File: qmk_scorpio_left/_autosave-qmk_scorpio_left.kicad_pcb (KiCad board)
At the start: 2 copper layers, 174.2 x 117.5 mm, 149 parts, among them J1 USB_C_Receptacle_USB2.0, J2 Conn_01x05, J3 USB_C_Receptacle_USB2.0, Q3 MMUN2133LT1G, U1 STM32G474CETx, U2 PRTR5V0U2X, U3 XC6206PxxxMR-Regulator_Linear, U4 CR2013-MI2120, U5 PRTR5V0U2X

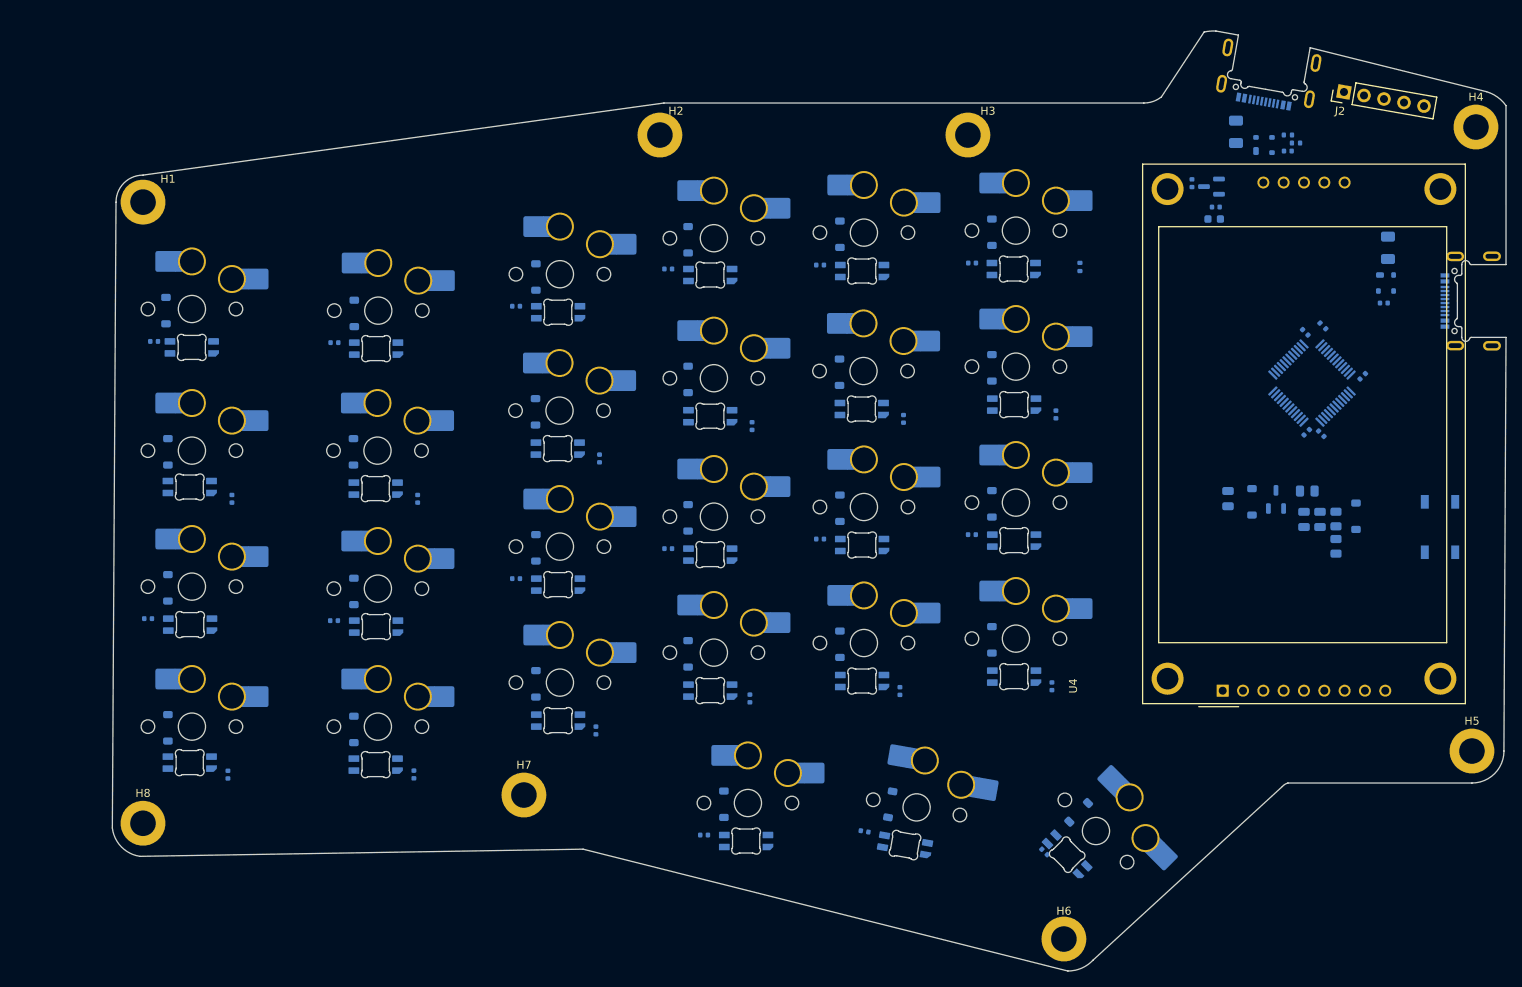
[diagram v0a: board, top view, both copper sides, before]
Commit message: fixed annular width drc error
increased pad diameter from 3.3 mm to 3.5 mm
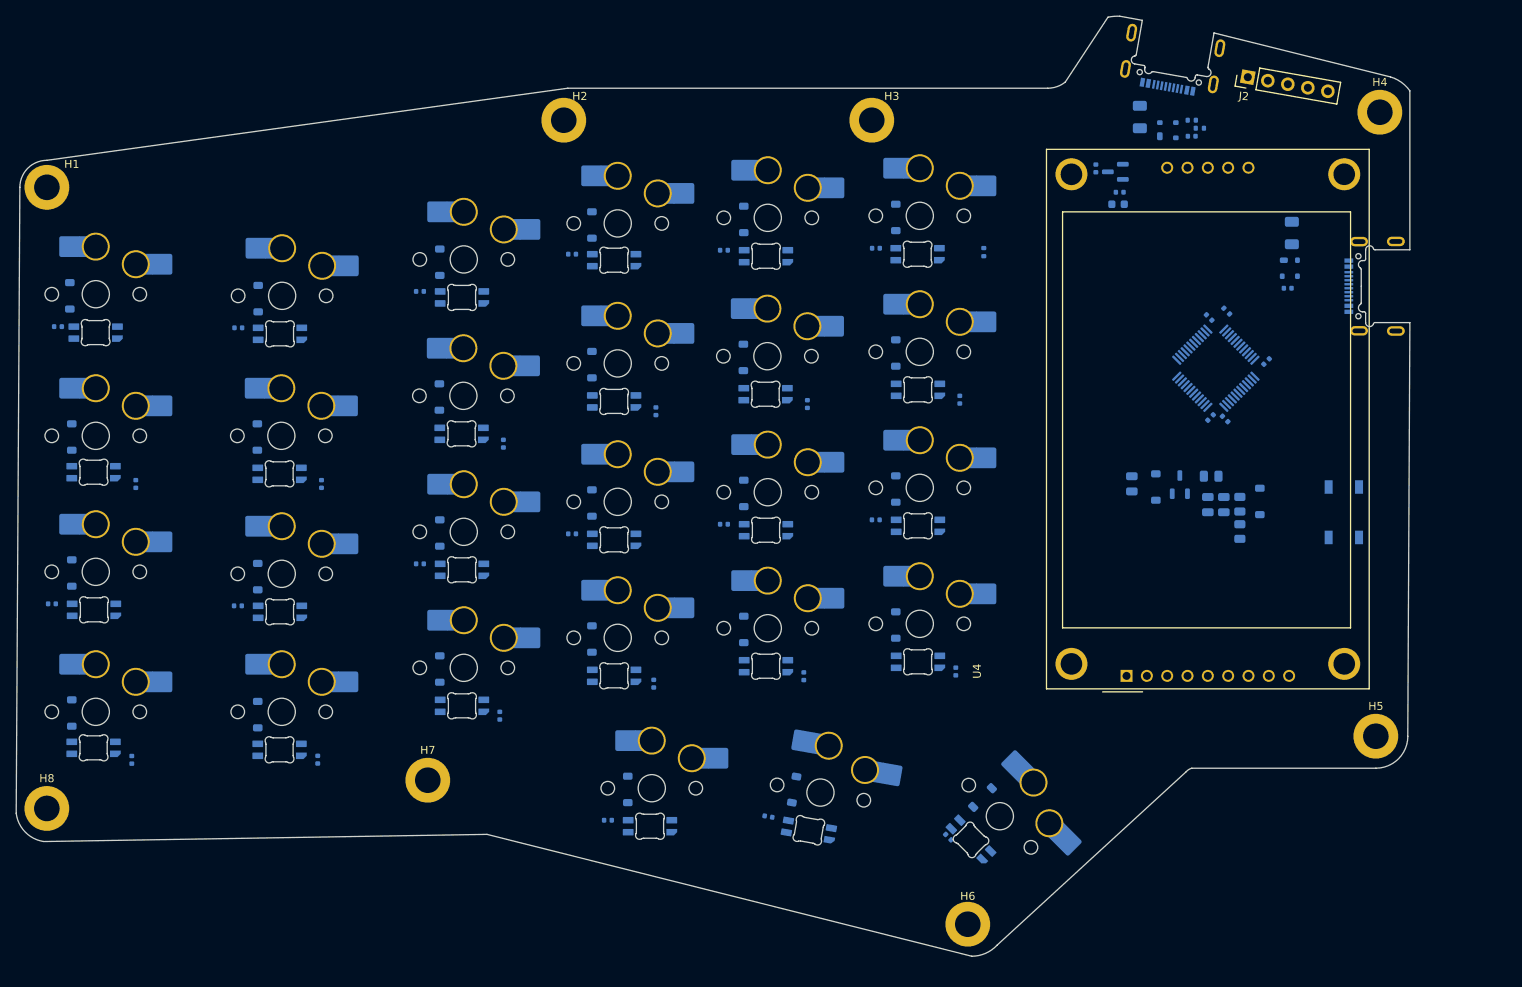
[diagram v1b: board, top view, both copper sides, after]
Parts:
- moved C27 12.2 mm to (179.6, 135.8)
- moved LED27 12.2 mm to (182.4, 136.1)
- moved C1 12.2 mm to (68.3, 72.0)
- moved C10 12.2 mm to (143.0, 82.5)
- moved C101 12.2 mm to (200.8, 56.6)
- moved C106 12.2 mm to (198.0, 52.2)
- moved C12 12.2 mm to (181.0, 81.1)
- moved C17 12.2 mm to (151.5, 96.7)
- moved C18 12.2 mm to (170.5, 96.1)
- moved C22 12.2 mm to (142.7, 116.6)
- moved C23 12.2 mm to (161.5, 115.7)
- moved C24 12.2 mm to (180.5, 115.1)
- moved C25 12.2 mm to (137.0, 133.7)
- moved C41 12.2 mm to (214.0, 94.2)
- moved C42 12.2 mm to (212.0, 94.2)
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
